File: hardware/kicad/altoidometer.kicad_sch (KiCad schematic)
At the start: 29 parts, among them J1 Conn_01x15_Pin, J2 AudioJack3, SW1 SW_Push, SW2 SW_Push, SW3 SW_Push, SW4 SW_Push, SW5 SW_Push, SW6 SW_Push, SW7 SW_Push, SW8 SW_Push, U1 DOIT-ESP32-DEVKIT-V1, U3 MAX44248ASA+, U4 MICROSD_SPI_OR_SDIO_CARD

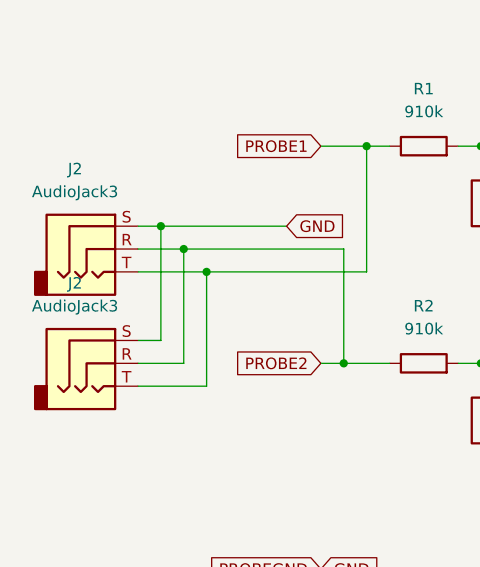
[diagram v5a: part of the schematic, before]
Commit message: fixed audio jack reference
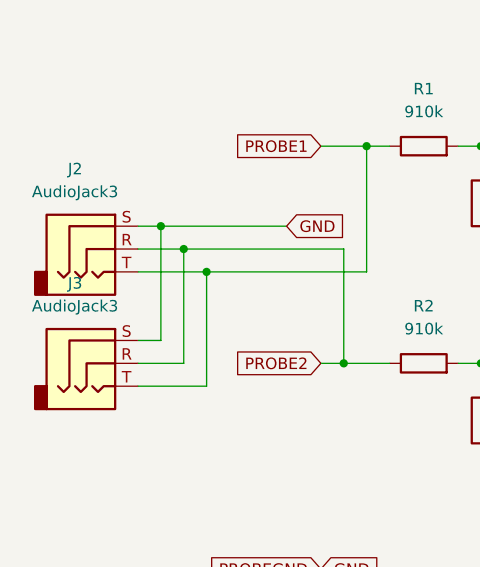
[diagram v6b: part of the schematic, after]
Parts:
- renumbered J2 to J3
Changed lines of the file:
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@@
 		(dnp no)
 		(fields_autoplaced yes)
-		(property "Reference" "J2"
+		(property "Reference" "J3"
 			(at 19.685 119.38 0)
 			(effects
@@
 			(project "altoidometer"
 				(path "/b57712fc-be2e-4ea6-81e8-e743779dbbdf"
-					(reference "J2")
+					(reference "J3")
 					(unit 1)
 				)
